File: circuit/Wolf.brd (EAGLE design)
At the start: 100 x 56 mm, 14 parts, among them IC1 74LS595N, K1 SNES, M1 ARDUINO-NANO-3.0

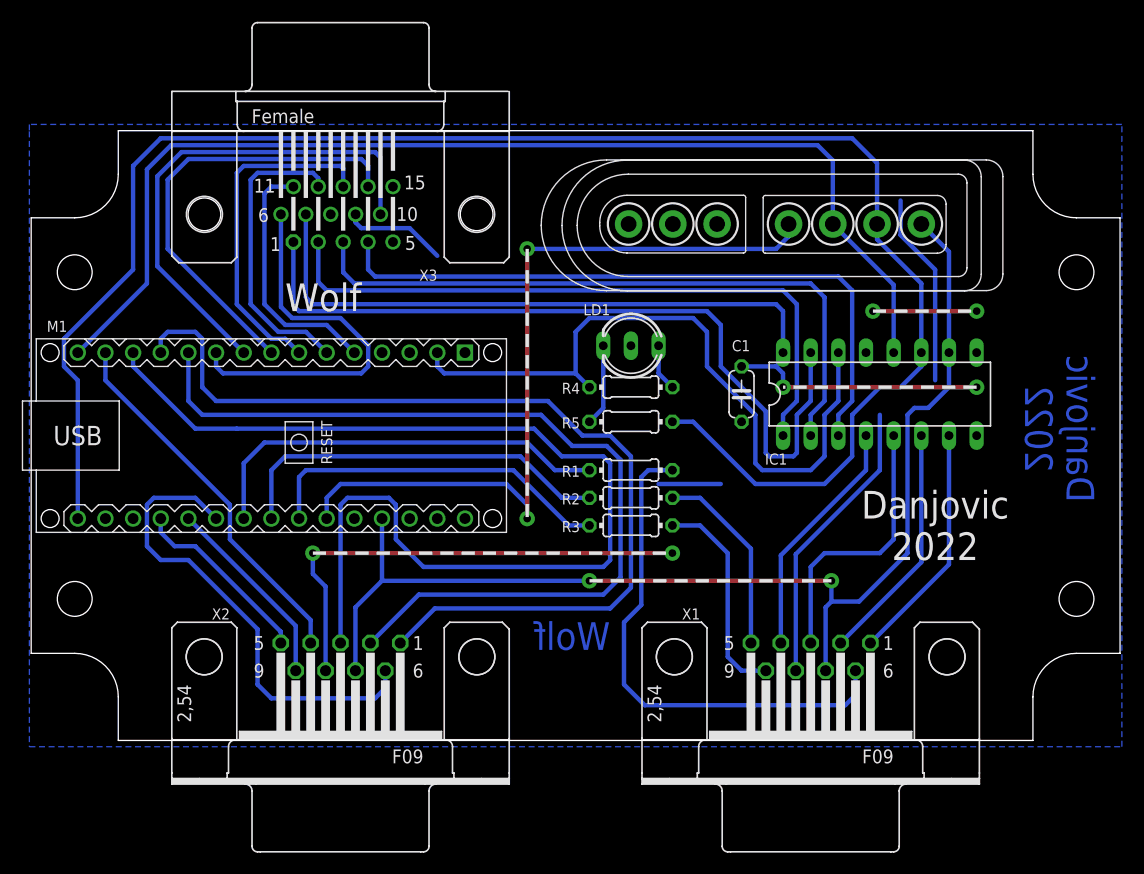
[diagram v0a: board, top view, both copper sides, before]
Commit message: added contention protect resistors
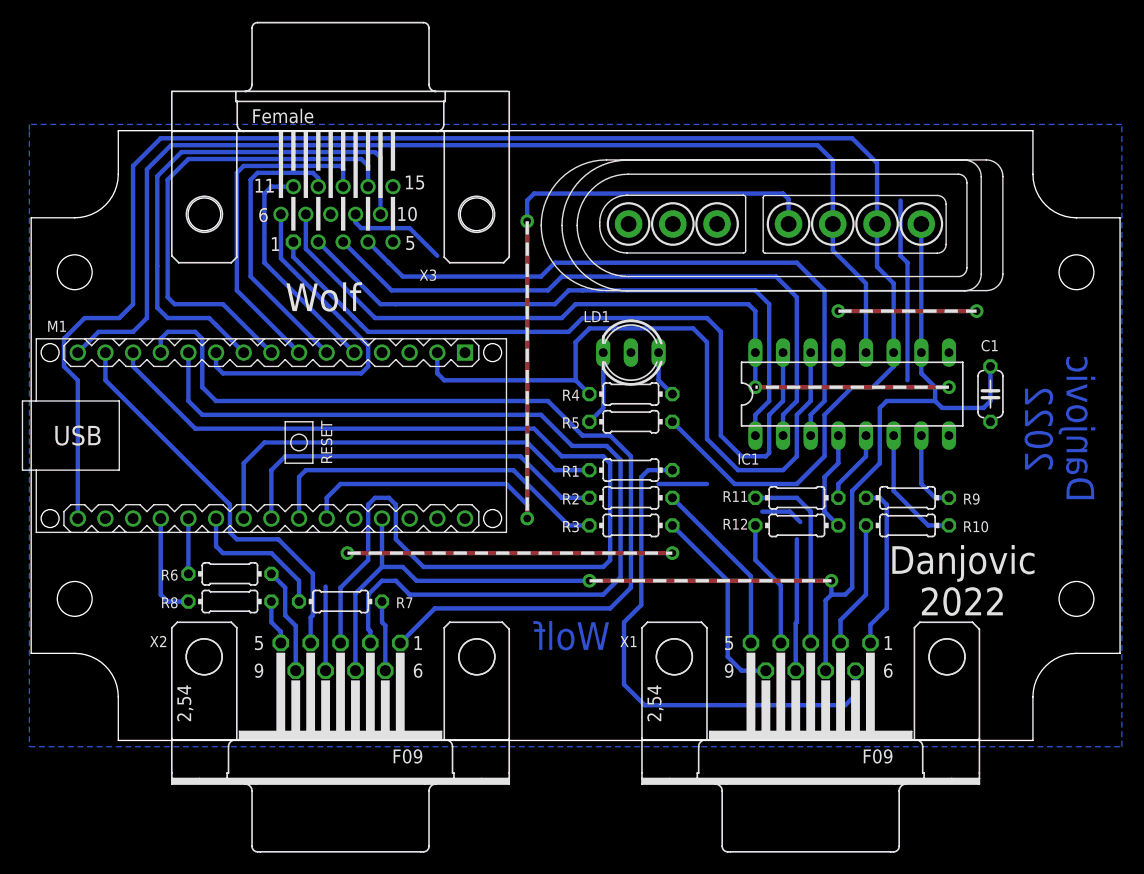
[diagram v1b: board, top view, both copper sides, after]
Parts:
- added R10, R11, R12, R6, R7, R8, R9: 560, rcl:0204/7
- moved C1 22.9 mm to (88.9, 31.8)
- moved IC1 2.54 mm to (76.2, 31.8)
- moved LD1 0.63 mm to (55.9, 35.6)
- moved R4 0.63 mm to (55.9, 31.8)
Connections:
- new net R_COL1: R6.2, X2.5
- new net R_COL2: R8.1, X2.9
- new net R_COL3: R7.1, X2.6
- new net R_DOWN: IC1.6, R10.1
- new net R_LEFT: IC1.5, R11.1
- new net R_RIGHT: IC1.4, R12.1
- new net R_UP: IC1.7, R9.1
- net COL1: now also R6.1; no longer X2.5
- net COL2: now also R8.2; no longer X2.9
- net COL3: now also R7.2; no longer X2.6
- net DOWN: now also R10.2; no longer IC1.6
- net LEFT: now also R11.2; no longer IC1.5
- net RIGHT: now also R12.2; no longer IC1.4
- net UP: now also R9.2; no longer IC1.7
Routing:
- net COL3: track 43.9 -> 13.4 mm
- net GND: track 113.6 -> 97.0 mm
- net COL2: track 18.1 -> 5.08 mm
- net R_DOWN: track 0.00 -> 11.5 mm
- net RIGHT: track 22.3 -> 11.8 mm
- net DOWN: track 22.1 -> 11.8 mm
- net R_COL2: track 0.00 -> 9.82 mm
- net R_RIGHT: track 0.00 -> 9.31 mm
- net R_UP: track 0.00 -> 7.51 mm
- net LEFT: track 25.2 -> 17.7 mm
- net COL1: track 17.1 -> 9.79 mm
- net R_LEFT: track 0.00 -> 6.77 mm
- net UP: track 22.0 -> 15.5 mm
- net R_COL3: track 0.00 -> 6.48 mm
- net DIN: track 73.3 -> 78.9 mm
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
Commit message: updated pcb
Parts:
- K1: device snes_breakout:SNESCONN -> snes_breakout:SNESCON-R
- moved LD1 38.6 mm to (92.7, 24.1), turned to 90 degrees
- moved R5 27.6 mm to (81.3, 40.0), turned to 0 degrees
- moved R4 18.3 mm to (71.1, 21.6)
- moved K1 15.8 mm to (82.5, 43.5), turned to 0 degrees
- moved R1 3.18 mm to (55.9, 21.6)
- moved R11 3.18 mm to (71.1, 19.1)
- moved R2 3.18 mm to (55.9, 19.1)
- moved R9 3.18 mm to (81.3, 19.1)
- moved R10 3.17 mm to (81.3, 16.5)
- moved R12 3.17 mm to (71.1, 16.5)
- moved R3 3.17 mm to (55.9, 16.5)
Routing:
- net GND: track 97.0 -> 134.6 mm, vias 4 -> 0
- net CLOCK: track 156.4 -> 126.8 mm
- net N$1: track 4.34 -> 26.7 mm
- net N$2: track 6.88 -> 23.8 mm
- net R_FIRE: track 47.5 -> 34.7 mm
- net DATA: track 62.2 -> 53.5 mm
- net LEFT: track 17.7 -> 13.4 mm
- net R_LEFT: track 6.77 -> 11.0 mm
- net R_RIGHT: track 9.31 -> 13.5 mm
- net UP: track 15.5 -> 11.6 mm
- net R_POT2: track 18.2 -> 14.7 mm
- net DIN: track 78.9 -> 82.2 mm
- net J3/J4: track 69.2 -> 65.9 mm
- net R_POT1: track 16.3 -> 13.1 mm
- net RIGHT: track 11.8 -> 8.59 mm
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
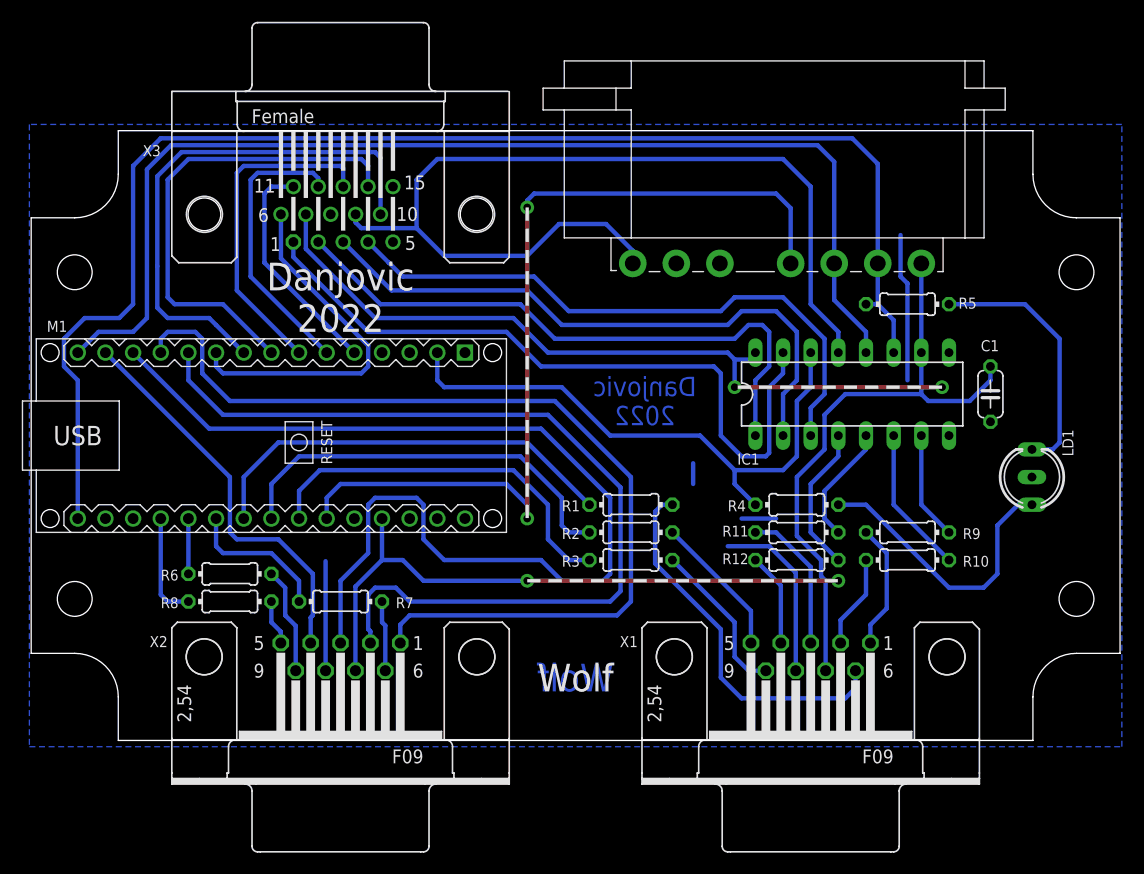
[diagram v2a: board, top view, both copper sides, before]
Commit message: Assed savekey eeprom to the circuit
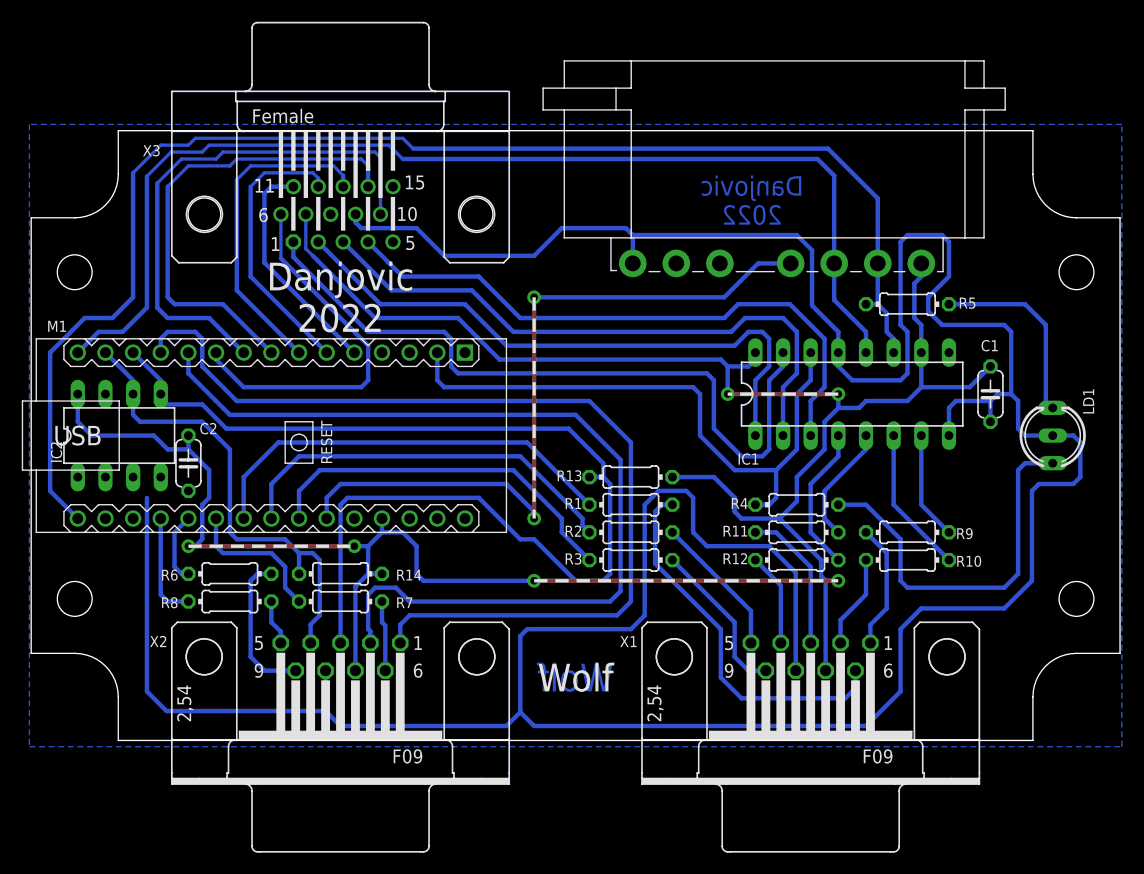
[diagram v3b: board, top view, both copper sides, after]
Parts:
- added C2: 100n, rcl:C050-024X044
- added IC2: 24LC256P, microchip:DIL8
- added R13, R14: 10k, rcl:0204/7
- moved LD1 4.26 mm to (94.6, 27.9)
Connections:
- removed net ROW3: M1.J1.13, X2.3
- removed net ROW4: M1.J1.14, X2.4
- new net ROW3/SDA: IC2.5, M1.J1.13, R13.1, X2.3
- new net ROW4/SCL: IC2.6, M1.J1.14, R14.1, X2.4
- net +5V: now also C2.1, IC2.8, R13.2, R14.2
- net GND: now also C2.2, IC2.1, IC2.2, IC2.3, IC2.4, IC2.7
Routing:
- net GND: track 134.6 -> 314.3 mm
- net ROW3/SDA: track 0.00 -> 101.3 mm
- net ROW3: track 97.8 -> 0.00 mm
- net +5V: track 187.6 -> 236.5 mm, vias 4 -> 6
- net ROW4/SCL: track 0.00 -> 43.8 mm
- net ROW4: track 36.9 -> 0.00 mm
- net DIN: track 82.2 -> 68.3 mm
- net N$1: track 26.7 -> 35.4 mm
- net N$2: track 23.8 -> 17.6 mm
- net R_COL2: track 9.82 -> 13.8 mm
- net DATA: track 53.5 -> 56.1 mm
- net LATCH: track 104.7 -> 103.1 mm
- net CLOCK: track 126.8 -> 125.3 mm
- net ROW1: track 87.3 -> 88.8 mm
- net B0/LP: track 33.1 -> 34.5 mm
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
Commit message: Added missing GND connection
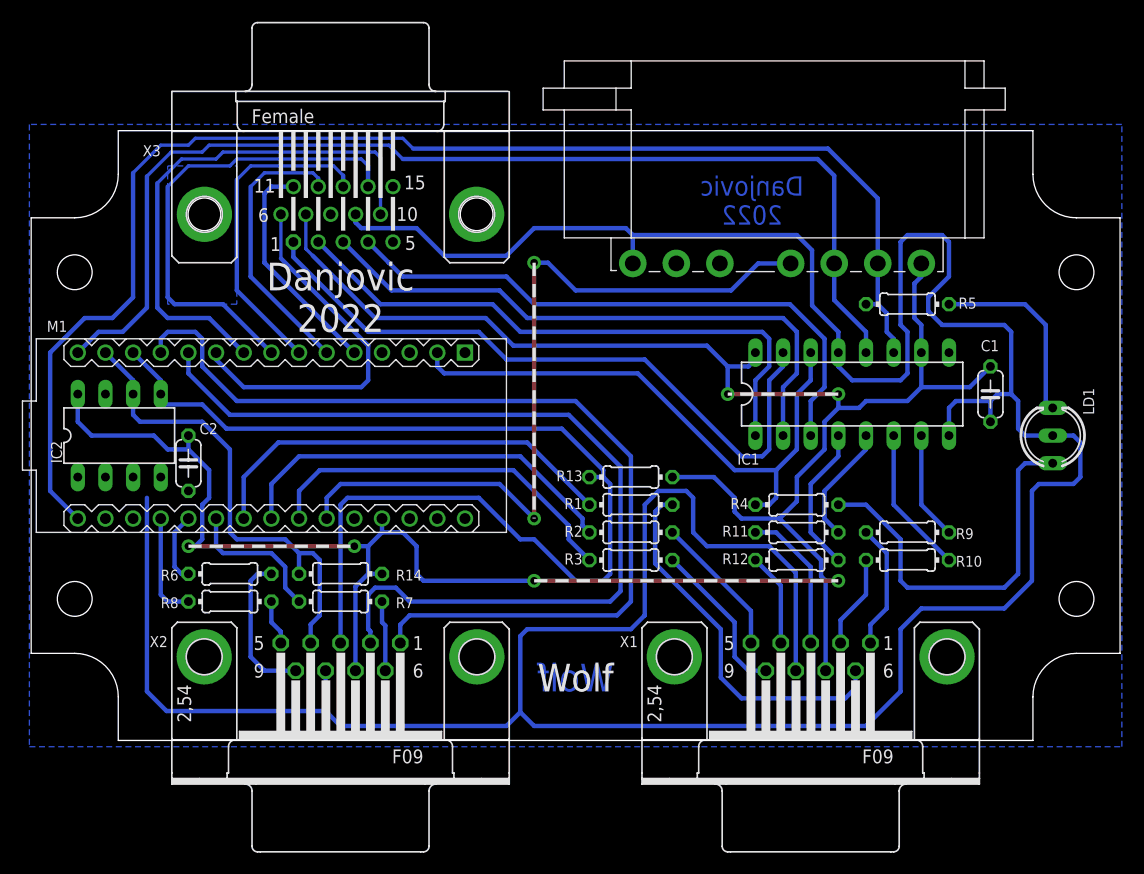
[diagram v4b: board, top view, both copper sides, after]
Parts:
- X1, X2: device con-subd:F09H -> con-subd:F09HP
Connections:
- removed net GND.1: M1.J1.4
- net GND: now also M1.J1.4
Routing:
- net J3/J4: track 66.4 -> 62.3 mm
- net DIN: track 68.3 -> 71.9 mm
- net DATA: track 56.1 -> 53.1 mm
- net J0/J7: track 56.1 -> 55.0 mm
- net J2/J5: track 55.6 -> 54.5 mm
- net J1/J6: track 56.2 -> 55.1 mm
- net ROW1: track 88.8 -> 88.0 mm
- added copper zone on layer 16, net N$3

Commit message: Changed resistor for bicolor LED
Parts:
- R4: value 2k2 -> 390
- R5: value 2k2 -> 560
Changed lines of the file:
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@@
 <attribute name="VALUE" x="54.8894" y="16.0274" size="0.9906" layer="27" ratio="10"/>
 </element>
-<element name="R4" library="rcl" package="0204/7" value="2k2" x="71.12" y="21.59" smashed="yes">
+<element name="R4" library="rcl" package="0204/7" value="390" x="71.12" y="21.59" smashed="yes">
 <attribute name="NAME" x="66.675" y="22.1996" size="1.016" layer="25" ratio="10" rot="R180"/>
 <attribute name="VALUE" x="70.1294" y="21.1074" size="0.9906" layer="27" ratio="10"/>
 </element>
-<element name="R5" library="rcl" package="0204/7" value="2k2" x="81.28" y="40.005" smashed="yes">
+<element name="R5" library="rcl" package="0204/7" value="560" x="81.28" y="40.005" smashed="yes">
 <attribute name="NAME" x="87.63" y="40.6146" size="1.016" layer="25" ratio="10" rot="R180"/>
 <attribute name="VALUE" x="82.2706" y="40.4876" size="0.9906" layer="27" ratio="10" rot="R180"/>

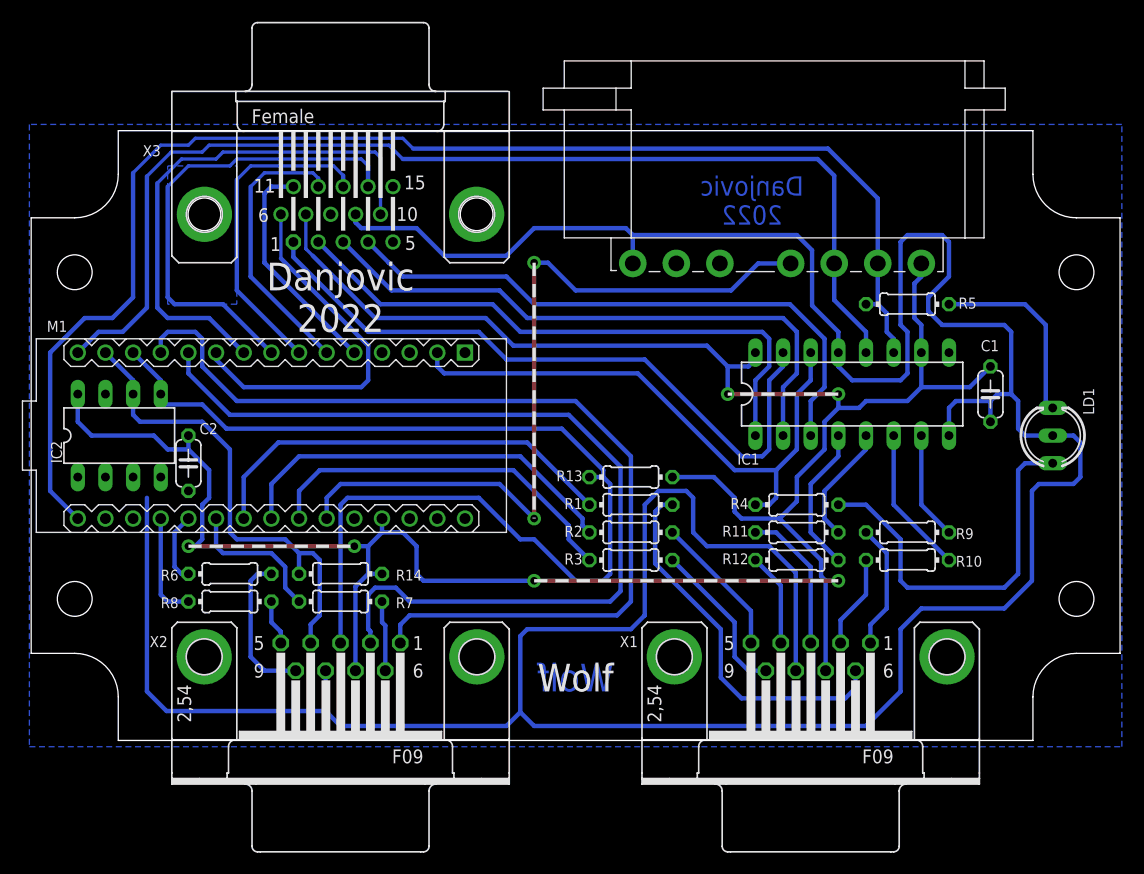
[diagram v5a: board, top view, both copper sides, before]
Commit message: Added neopixel to indicate operating mode
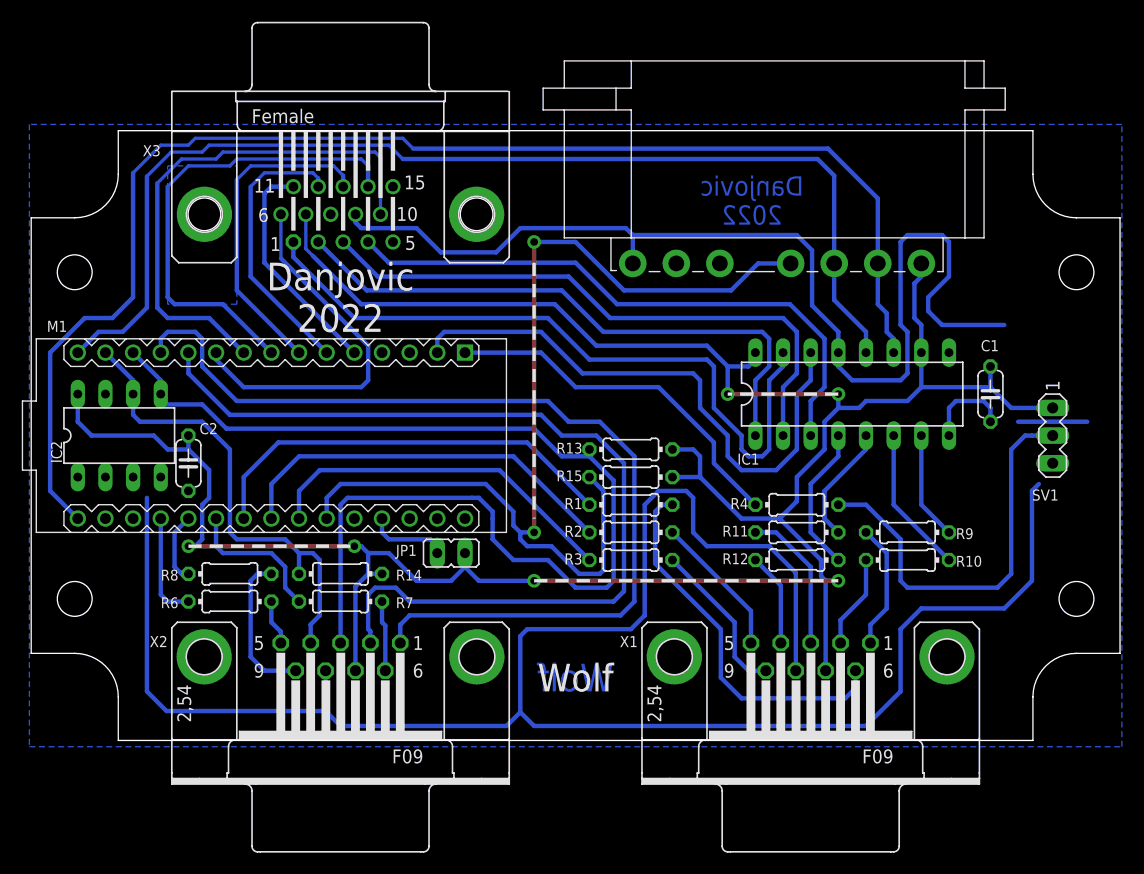
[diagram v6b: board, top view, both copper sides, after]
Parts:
- removed LD1: (no value), led:DUOLED-C-5MM
- removed R5: 560, rcl:0204/7
- added JP1: (no value), jumper:JP1
- added R15: 10k, rcl:0204/7
- added SV1: (no value), con-lstb:MA03-1
- moved R13 2.54 mm to (55.9, 26.7)
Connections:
- removed net N$2: LD1.AR, R5.2
- new net LED: M1.J1.1, R4.1
- new net VCC_ARD: JP1.1, M1.J2.4
- net +5V: now also JP1.2, R15.2, SV1.1; no longer M1.J2.4
- net CLOCK: no longer R5.1
- net DATA: no longer R4.1
- net DIN: now also R15.1
- net GND: now also SV1.3; no longer LD1.C
- net N$1: now also SV1.2; no longer LD1.AX
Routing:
- net LED: track 0.00 -> 33.6 mm
- net DIN: track 71.9 -> 96.0 mm
- net GND: track 314.3 -> 294.3 mm
- net N$2: track 17.6 -> 0.00 mm
- net +5V: track 236.5 -> 246.0 mm
- net VCC_ARD: track 0.00 -> 7.51 mm
- net J3/J4: track 62.3 -> 65.3 mm
- net ROW3/SDA: track 101.0 -> 103.2 mm
- net N$1: track 35.4 -> 37.6 mm
- net CLOCK: track 125.3 -> 124.2 mm
- net ROW2: track 85.5 -> 86.3 mm
- net POT2: track 34.2 -> 33.4 mm
- net ROW1: track 88.0 -> 88.6 mm
- net DATA: track 53.1 -> 52.6 mm
